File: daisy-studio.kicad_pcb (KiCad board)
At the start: 4 copper layers, 278.3 x 56.7 mm, 149 parts, among them J1 NCJ6FA-H-0, J10 SDS-50J, J11 Conn_02x12_Odd_Even, J12 Conn_02x02_Odd_Even, J13 Barrel_Jack_MountingPin, J14 Micro_SD_Card_Det2, J2 NCJ6FA-H-0, J3 Conn_02x10_Odd_Even, J4 NCJ6FA-H-0, J5 Conn_02x10_Odd_Even, J6 NCJ6FA-H-0, J7 SDS-50J, J9 SDS-50J, Q1 MMBT3904, Q2 MMBT3906, Q3 MMBT3906, Q4 MMBT3904, Q5 DMP3056L-13, SW1 Power, U1 THAT1646, U10 TPS54302, U2 THAT1646, U3 OPA1656ID, U4 THAT1246, U5 THAT1246, U6 OPA1656ID, U7 LM2903, U8 H11L1, U9 Daisy_Seed

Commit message: fix ground #13
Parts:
- removed H6: MountingHole, MountingHole:MountingHole_3.2mm_M3
- added H9: MountingHole, MountingHole:MountingHole_3.2mm_M3, F.Cu at (57.1, 54.1)
- J11: value Conn_02x12_Odd_Even -> Conn_02x14_Odd_Even
- J8: value ~ -> Conn_02x03
- moved D9 0.16 mm to (54.4, 60.1)
- moved J5 0.12 mm to (31.6, 65.7)
- moved D10 0.10 mm to (54.4, 73.6)
- moved RV5 0.10 mm to (38.6, 58.6)
- moved RV1 0.06 mm to (38.6, 31.4)
- moved RV6 0.06 mm to (38.6, 72.4)
- moved RV3 0.05 mm to (38.6, 45.2)
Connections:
- D14 pad 2: Net-(D14-A2) -> GND
- J13 pad 2: Net-(D14-A2) -> GND
- R33 pad 2: Net-(D14-A2) -> GND
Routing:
- net GND: track 228.6 -> 239.2 mm
- net Net-(D14-A2): track 10.6 -> 0.00 mm

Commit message: Fix reverse polarity mosfet
closes #14
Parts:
- removed H9: MountingHole, MountingHole:MountingHole_3.2mm_M3
- added H3: MountingHole, MountingHole:MountingHole_3.2mm_M3, F.Cu at (57.1, 54.1)
- moved Q5 0.74 mm to (278.9, 36.3), turned to -90 degrees
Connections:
- Q5 pad 2: Net-(Q5-S) -> +12V_RAW
- Q5 pad 3: +12V_RAW -> Net-(Q5-D)
- SW1 pad 2: Net-(Q5-S) -> Net-(Q5-D)
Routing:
- net Net-(Q5-S): track 26.3 -> 0.00 mm
- net Net-(Q5-D): track 0.00 -> 25.0 mm
- net +12V_RAW: track 70.0 -> 74.2 mm
- net Net-(Q5-G): track 5.17 -> 2.98 mm
- net GND: vias 2193 -> 2192

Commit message: r_fb_fixed changed to 6.8k
closes #15
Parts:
- R2, R7: value 15k -> 6.8k
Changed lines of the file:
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@@
 			)
 		)
-		(property "Value" "15k"
+		(property "Value" "6.8k"
 			(at 0 1.65 90)
 			(layer "F.Fab")
@@
 			)
 		)
-		(property "Value" "15k"
+		(property "Value" "6.8k"
 			(at 0 1.65 90)
 			(layer "F.Fab")

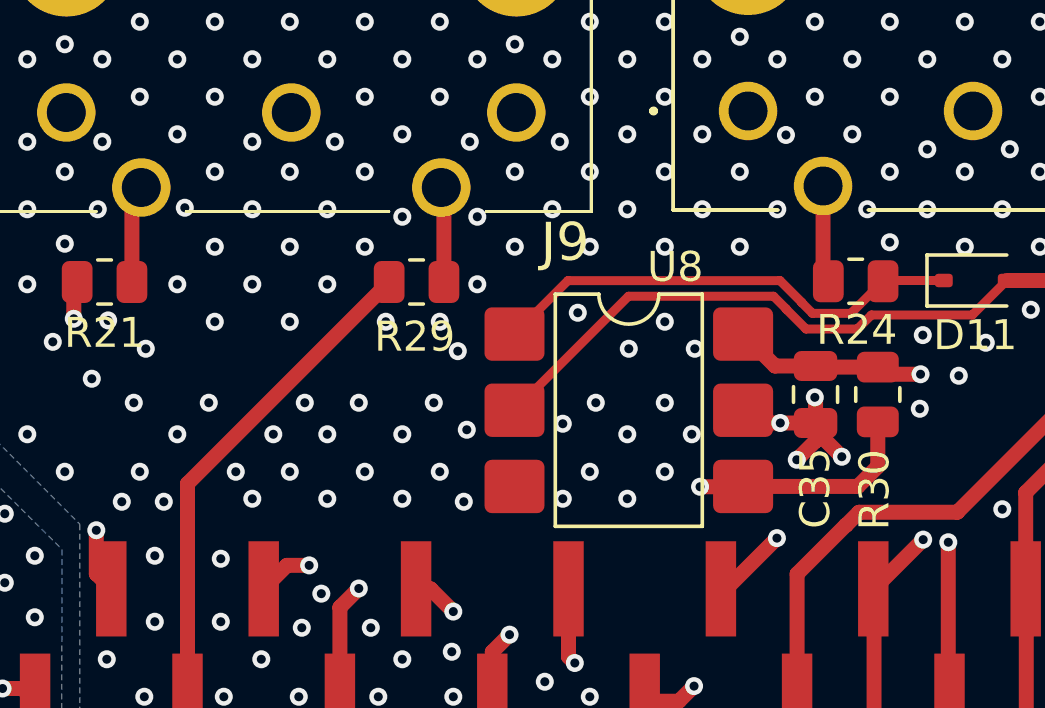
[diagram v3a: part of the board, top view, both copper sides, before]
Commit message: make optocoupler pads longer for hand soldering
fixes: 17
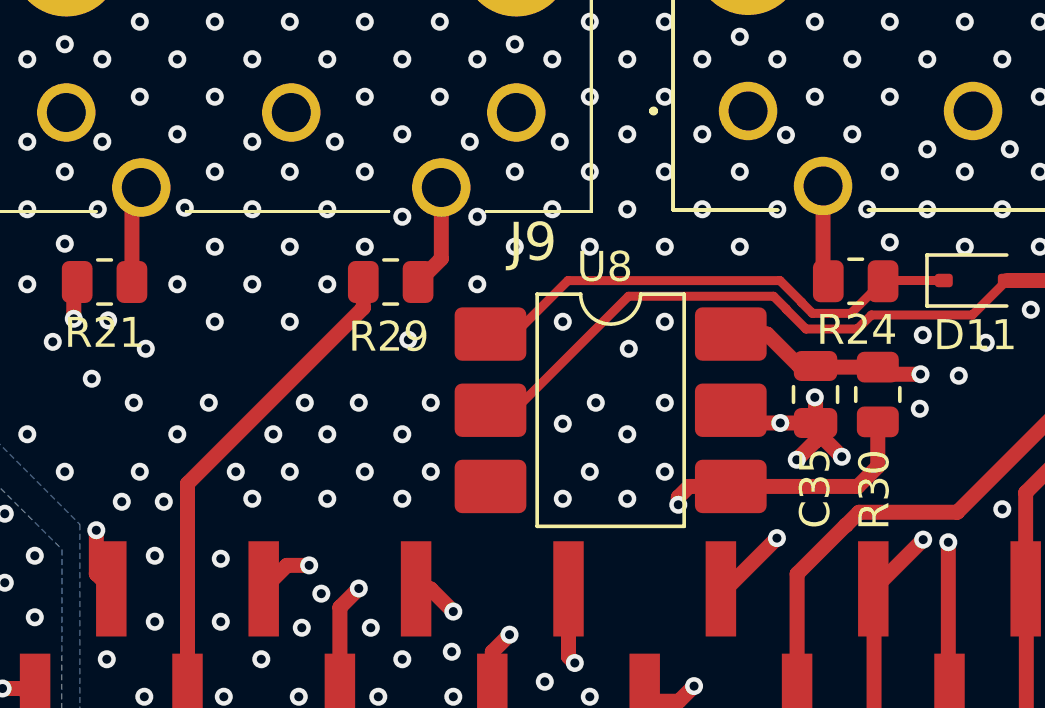
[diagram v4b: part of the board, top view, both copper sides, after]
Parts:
- moved R29 0.86 mm to (228.1, 43.5)
- moved U8 0.60 mm to (235.4, 47.8)
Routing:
- net GND: track 239.2 -> 240.2 mm, vias 2192 -> 2186
- net +3V3D: track 147.6 -> 148.2 mm
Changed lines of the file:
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@@
 		(tags "Connector")
 		(property "Reference" "J9"
-			(at -16.625 -4.325 0)
+			(at -15.55 -4.325 0)
 			(layer "F.SilkS")
 			(effects
@@
 	(footprint "Package_DIP:SMDIP-6_W7.62mm"
 		(layer "F.Cu")
-		(at 236 47.75)
+		(at 235.395 47.75)
 		(descr "6-lead surface-mounted (SMD) DIP package, row spacing 7.62mm (300 mils)")
 		(tags "SMD DIP DIL PDIP SMDIP 2.54mm 7.62mm 300mil")
 		(property "Reference" "U8"
-			(at 1.55 -4.775 0)
+			(at -0.195 -4.775 0)
 			(layer "F.SilkS")
 			(effects
@@
 		)
 		(fp_rect
-			(start -5.07 -4.06)
-			(end 5.07 4.06)
+			(start -5.47 -4.06)
+			(end 5.47 4.06)
 			(stroke
 				(width 0.05)
@@
 		)
 		(pad "1" smd roundrect
-			(at -3.81 -2.54)
-			(size 2 1.78)
+			(at -4.005 -2.54)
+			(size 2.39 1.78)
 			(layers "F.Cu" "F.Mask" "F.Paste")
 			(roundrect_rratio 0.140449)
@@
 		)
 		(pad "2" smd roundrect
-			(at -3.81 0)
-			(size 2 1.78)
+			(at -4.005 0)
+			(size 2.39 1.78)
 			(layers "F.Cu" "F.Mask" "F.Paste")
 			(roundrect_rratio 0.140449)
@@
 		)
 		(pad "3" smd roundrect
-			(at -3.81 2.54)
-			(size 2 1.78)
+			(at -4.005 2.54)
+			(size 2.39 1.78)
 			(layers "F.Cu" "F.Mask" "F.Paste")
 			(roundrect_rratio 0.140449)
@@
 		)
 		(pad "4" smd roundrect
-			(at 3.81 2.54)
-			(size 2 1.78)
+			(at 4.005 2.54)
+			(size 2.39 1.78)
 			(layers "F.Cu" "F.Mask" "F.Paste")
 			(roundrect_rratio 0.140449)
@@
 		)
 		(pad "5" smd roundrect
-			(at 3.81 0)
-			(size 2 1.78)
+			(at 4.005 0)
+			(size 2.39 1.78)
 			(layers "F.Cu" "F.Mask" "F.Paste")
 			(roundrect_rratio 0.140449)
@@
 		)
 		(pad "6" smd roundrect
-			(at 3.81 -2.54)
-			(size 2 1.78)
+			(at 4.005 -2.54)
+			(size 2.39 1.78)
 			(layers "F.Cu" "F.Mask" "F.Paste")
 			(roundrect_rratio 0.140449)
@@
 	(footprint "Resistor_SMD:R_0805_2012Metric"
 		(layer "F.Cu")
-		(at 228.925 43.475 180)
+		(at 228.0625 43.475 180)
 		(descr "Resistor SMD 0805 (2012 Metric), square (rectangular) end terminal, IPC-7351 nominal, (Body size source: IPC-SM-782 page 72, https://www.pcb-3d.com/wordpress/wp-content/uploads/ipc-sm-782a_amendment_1_and_2.pdf), generated with kicad-footprint-generator")
 		(tags "resistor")
@@
 	)
 	(segment
+		(start 239.825 48.175)
+		(end 239.4 47.75)
+		(width 0.5)
+		(layer "F.Cu")
+		(net 1)
+	)
+	(segment
 		(start 292.27 50.95)
 		(end 292.58 50.95)
@@
 	)
 	(segment
+		(start 241.05 48.175)
+		(end 239.825 48.175)
+		(width 0.5)
+		(layer "F.Cu")
+		(net 1)
+	)
+	(segment
 		(start 281.525 80.475)
 		(end 282.2 79.8)
@@
 	)
 	(segment
-		(start 241.05 48.175)
-		(end 240.235 48.175)
-		(width 0.5)
-		(layer "F.Cu")
-		(net 1)
-	)
-	(segment
 		(start 190.05 48.55)
 		(end 189.45 49.15)
@@
 	)
 	(via
-		(at 234.3 44.5)
+		(at 233.8 44.8)
 		(size 0.6)
 		(drill 0.3)
@@
 	)
 	(via
-		(at 227.9 44.8)
+		(at 228.65 45.4)
 		(size 0.6)
 		(drill 0.3)
@@
 	)
 	(via
-		(at 230.5 50.8)
-		(size 0.6)
-		(drill 0.3)
-		(layers "F.Cu" "B.Cu")
-		(free yes)
-		(net 1)
-	)
-	(via
 		(at 263.45 31.05)
 		(size 0.6)
@@
 	)
 	(via
-		(at 238.2 45.7)
-		(size 0.6)
-		(drill 0.3)
-		(layers "F.Cu" "B.Cu")
-		(free yes)
-		(net 1)
-	)
-	(via
 		(at 72.2 79.8)
 		(size 0.6)
@@
 	)
 	(via
-		(at 229.7 49.8)
+		(at 229.4 49.8)
 		(size 0.6)
 		(drill 0.3)
@@
 	)
 	(via
-		(at 229.5 47.5)
+		(at 229.4 47.5)
 		(size 0.6)
 		(drill 0.3)
@@
 	)
 	(via
-		(at 230.3 45.78)
-		(size 0.6)
-		(drill 0.3)
-		(layers "F.Cu" "B.Cu")
-		(free yes)
-		(net 1)
-	)
-	(via
 		(at 203.7 71.05)
 		(size 0.6)
@@
 	)
 	(via
-		(at 229.7 44.8)
-		(size 0.6)
-		(drill 0.3)
-		(layers "F.Cu" "B.Cu")
-		(free yes)
-		(net 1)
-	)
-	(via
 		(at 199.7 44.8)
 		(size 0.6)
@@
 	)
 	(via
-		(at 230.6 48.4)
-		(size 0.6)
-		(drill 0.3)
-		(layers "F.Cu" "B.Cu")
-		(free yes)
-		(net 1)
-	)
-	(via
 		(at 124.1 77.3)
 		(size 0.6)
@@
 	)
 	(via
-		(at 238.1 48.55)
-		(size 0.6)
-		(drill 0.3)
-		(layers "F.Cu" "B.Cu")
-		(free yes)
-		(net 1)
-	)
-	(via
 		(at 51.4 77.4)
 		(size 0.6)
@@
 	)
 	(segment
-		(start 240.875 46.275)
-		(end 239.81 45.21)
-		(width 0.5)
-		(layer "F.Cu")
-		(net 16)
-	)
-	(segment
 		(start 250.275 63.245)
 		(end 250.1575 63.245)
@@
 	)
 	(segment
-		(start 242.06 46.275)
-		(end 240.875 46.275)
+		(start 240.61 45.21)
+		(end 241.675 46.275)
 		(width 0.5)
 		(layer "F.Cu")
@@
 	)
 	(segment
+		(start 239.4 45.21)
+		(end 240.61 45.21)
+		(width 0.5)
+		(layer "F.Cu")
+		(net 16)
+	)
+	(segment
+		(start 241.675 46.275)
+		(end 242.225 46.275)
+		(width 0.5)
+		(layer "F.Cu")
+		(net 16)
+	)
+	(segment
 		(start 250.1575 63.245)
 		(end 249.25 62.3375)
@@
 	)
 	(segment
-		(start 229.8375 43.475)
-		(end 229.8375 40.4125)
+		(start 229.75 42.7)
+		(end 229.75 40.325)
+		(width 0.5)
+		(layer "F.Cu")
+		(net 49)
+	)
+	(segment
+		(start 228.975 43.475)
+		(end 229.75 42.7)
 		(width 0.5)
 		(layer "F.Cu")
@@
 	)
 	(segment
-		(start 228.0125 43.475)
-		(end 221.29 50.1975)
+		(start 221.29 50.1975)
+		(end 227.15 44.3375)
+		(width 0.5)
+		(layer "F.Cu")
+		(net 57)
+	)
+	(segment
+		(start 227.15 44.3375)
+		(end 227.15 43.475)
 		(width 0.5)
 		(layer "F.Cu")
@@
 	)
 	(segment
-		(start 239.81 50.29)
-		(end 243.635 50.29)
+		(start 238.01 50.29)
+		(end 239.4 50.29)
 		(width 0.5)
 		(layer "F.Cu")
@@
 	)
 	(segment
+		(start 237.65 50.9)
+		(end 237.65 50.65)
+		(width 0.5)
+		(layer "F.Cu")
+		(net 58)
+	)
+	(segment
 		(start 208.9 43.425)
 		(end 209.925 43.425)
@@
 	(segment
 		(start 243.635 50.29)
+		(end 239.4 50.29)
+		(width 0.5)
+		(layer "F.Cu")
+		(net 58)
+	)
+	(segment
+		(start 243.635 50.29)
 		(end 244.3 49.625)
 		(width 0.5)
@@
 	)
 	(segment
-		(start 238.375 50.3)
-		(end 239.8 50.3)
+		(start 237.65 50.65)
+		(end 238.01 50.29)
 		(width 0.5)
 		(layer "F.Cu")
@@
 	)
 	(via
-		(at 238.375 50.3)
+		(at 237.65 50.9)
 		(size 0.6)
 		(drill 0.3)
@@
 	)
 	(segment
-		(start 218.25 51.75)
-		(end 236.925 51.75)
+		(start 237.3 51.75)
+		(end 237.65 51.4)
 		(width 0.5)
 		(layer "In1.Cu")
@@
 	)
 	(segment
-		(start 209.925 43.425)
-		(end 213.175 43.425)
+		(start 237.65 51.4)
+		(end 237.65 50.9)
 		(width 0.5)
 		(layer "In1.Cu")
@@
 	)
 	(segment
-		(start 213.175 43.425)
-		(end 218.25 48.5)
+		(start 218.25 51.75)
+		(end 237.3 51.75)
 		(width 0.5)
 		(layer "In1.Cu")
@@
 	)
 	(segment
-		(start 236.925 51.75)
-		(end 238.375 50.3)
+		(start 209.925 43.425)
+		(end 213.175 43.425)
+		(width 0.5)
+		(layer "In1.Cu")
+		(net 58)
+	)
+	(segment
+		(start 213.175 43.425)
+		(end 218.25 48.5)
 		(width 0.5)
 		(layer "In1.Cu")
